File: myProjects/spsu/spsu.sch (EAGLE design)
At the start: 21 parts, among them IC1 MC34063A, J1 12V-in, J2 Hi-V, Q1 IRF840, X1 PJ-102A, X2 PJ-102A

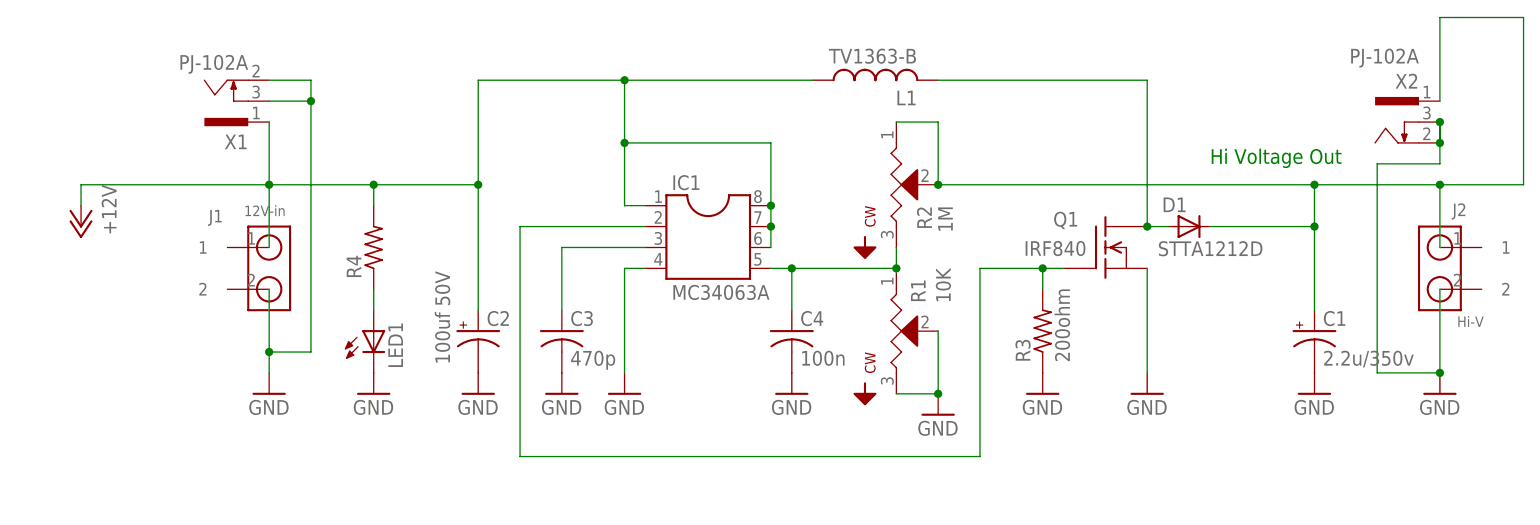
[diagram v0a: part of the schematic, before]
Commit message: removed power plugs and replaces with molex added Gerber files
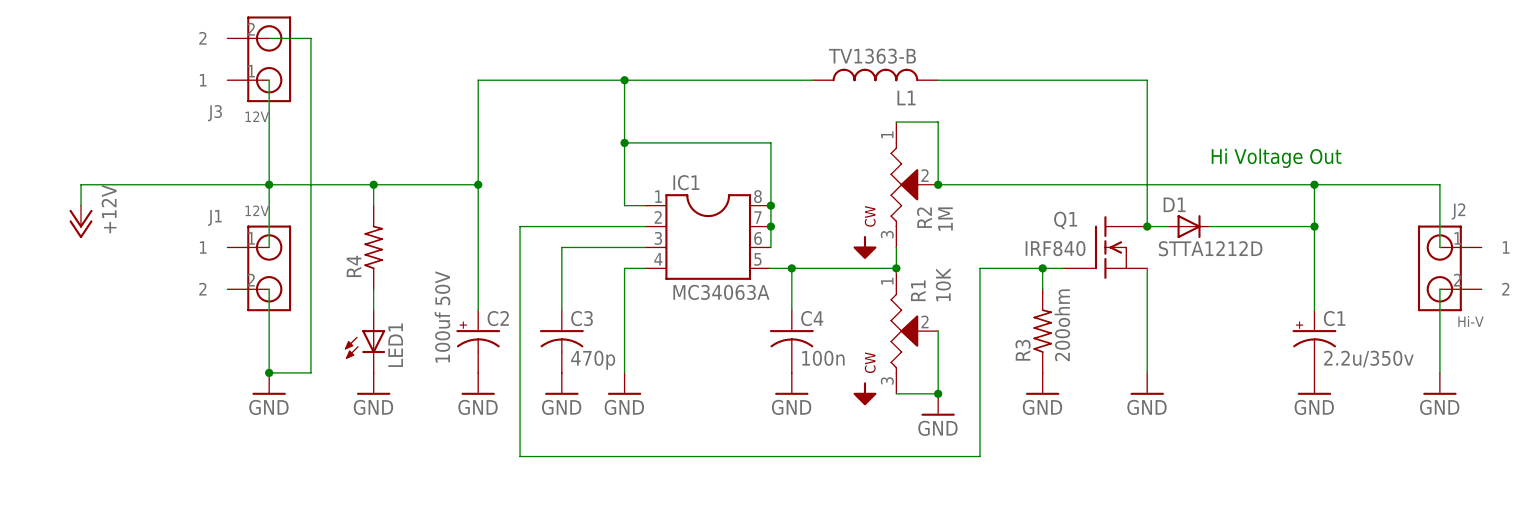
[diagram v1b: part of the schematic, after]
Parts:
- removed X1, X2: PJ-102A, kmarx1:PJ-102A
- added J3: 12V, kmarx1:MOLEX-2PIN-BASE
- J1: value 12V-in -> 12V
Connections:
- net +12V: now also J3.1; no longer X1.1
- net GND: now also J3.2; no longer X1.2, X1.3, X2.2, X2.3
- net HIVOLTAGEOUT: no longer X2.1
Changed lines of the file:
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@@
 <?xml version="1.0" encoding="utf-8"?>
 <!DOCTYPE eagle SYSTEM "eagle.dtd">
-<eagle version="6.0">
+<eagle version="6.1">
 <drawing>
 <settings>
@@
 <part name="R3" library="rcl" deviceset="R-US_" device="0204/5" value="200ohm"/>
 <part name="GND1" library="supply1" deviceset="GND" device=""/>
-<part name="J1" library="kmarx1" deviceset="MOLEX-2PIN-BASE" device="" value="12V-in"/>
+<part name="J1" library="kmarx1" deviceset="MOLEX-2PIN-BASE" device="" value="12V"/>
 <part name="J2" library="kmarx1" deviceset="MOLEX-2PIN-BASE" device="" value="Hi-V"/>
 <part name="GND2" library="supply1" deviceset="GND" device=""/>
@@
 <part name="H3" library="holes" deviceset="MOUNT-HOLE" device="3.0"/>
 <part name="H4" library="holes" deviceset="MOUNT-HOLE" device="3.0"/>
-<part name="X1" library="kmarx1" deviceset="PJ-102*" device="" technology="A"/>
-<part name="X2" library="kmarx1" deviceset="PJ-102*" device="" technology="A"/>
 <part name="LED1" library="led" deviceset="LED" device="3MM"/>
 <part name="GND11" library="supply1" deviceset="GND" device=""/>
 <part name="R4" library="rcl" deviceset="R-US_" device="0204/5"/>
+<part name="J3" library="kmarx1" deviceset="MOLEX-2PIN-BASE" device="" value="12V"/>
 </parts>
 <sheets>
@@
 <instance part="H3" gate="G$1" x="7.62" y="15.24"/>
 <instance part="H4" gate="G$1" x="7.62" y="7.62"/>
-<instance part="X1" gate="G$1" x="63.5" y="114.3" rot="R180"/>
-<instance part="X2" gate="G$1" x="205.74" y="111.76" smashed="yes" rot="MR0">
-<attribute name="NAME" x="208.28" y="115.824" size="1.778" layer="95" rot="MR0"/>
-<attribute name="VALUE" x="208.28" y="118.872" size="1.778" layer="96" rot="MR0"/>
-</instance>
 <instance part="LED1" gate="G$1" x="81.28" y="86.36"/>
 <instance part="GND11" gate="1" x="81.28" y="78.74"/>
 <instance part="R4" gate="G$1" x="81.28" y="96.52" rot="R90"/>
+<instance part="J3" gate="G$1" x="68.58" y="119.38" smashed="yes" rot="MR180">
+<attribute name="NAME" x="62.992" y="112.268" size="1.524" layer="95" font="vector" rot="MR0"/>
+<attribute name="VALUE" x="65.532" y="113.03" size="1.27" layer="95" font="vector" rot="MR180"/>
+</instance>
 </instances>
 <busses>
@@
 </segment>
 <segment>
-<wire x1="68.58" y1="116.84" x2="73.66" y2="116.84" width="0.1524" layer="91"/>
-<wire x1="73.66" y1="116.84" x2="73.66" y2="114.3" width="0.1524" layer="91"/>
-<wire x1="73.66" y1="114.3" x2="73.66" y2="83.82" width="0.1524" layer="91"/>
-<wire x1="68.58" y1="91.44" x2="68.58" y2="83.82" width="0.1524" layer="91"/>
-<wire x1="68.58" y1="83.82" x2="68.58" y2="81.28" width="0.1524" layer="91"/>
-<wire x1="73.66" y1="83.82" x2="68.58" y2="83.82" width="0.1524" layer="91"/>
-<wire x1="68.58" y1="114.3" x2="73.66" y2="114.3" width="0.1524" layer="91"/>
-<junction x="68.58" y="83.82"/>
-<junction x="73.66" y="114.3"/>
+<wire x1="68.58" y1="91.44" x2="68.58" y2="81.28" width="0.1524" layer="91"/>
 <pinref part="GND10" gate="1" pin="GND"/>
 <pinref part="J1" gate="G$1" pin="2"/>
-<pinref part="X1" gate="G$1" pin="2"/>
-<pinref part="X1" gate="G$1" pin="3"/>
-</segment>
-<segment>
-<wire x1="210.82" y1="111.76" x2="210.82" y2="109.22" width="0.1524" layer="91"/>
-<wire x1="210.82" y1="109.22" x2="210.82" y2="106.68" width="0.1524" layer="91"/>
-<wire x1="210.82" y1="106.68" x2="203.2" y2="106.68" width="0.1524" layer="91"/>
-<wire x1="203.2" y1="106.68" x2="203.2" y2="81.28" width="0.1524" layer="91"/>
+<pinref part="J3" gate="G$1" pin="2"/>
+<wire x1="68.58" y1="121.92" x2="73.66" y2="121.92" width="0.1524" layer="91"/>
+<wire x1="73.66" y1="121.92" x2="73.66" y2="81.28" width="0.1524" layer="91"/>
+<wire x1="73.66" y1="81.28" x2="68.58" y2="81.28" width="0.1524" layer="91"/>
+<junction x="68.58" y="81.28"/>
+</segment>
+<segment>
 <wire x1="210.82" y1="91.44" x2="210.82" y2="81.28" width="0.1524" layer="91"/>
-<wire x1="203.2" y1="81.28" x2="210.82" y2="81.28" width="0.1524" layer="91"/>
-<wire x1="210.82" y1="111.76" x2="210.82" y2="109.22" width="0.1524" layer="91"/>
-<junction x="210.82" y="81.28"/>
-<junction x="210.82" y="109.22"/>
-<junction x="210.82" y="111.76"/>
 <pinref part="GND1" gate="1" pin="GND"/>
 <pinref part="J2" gate="G$1" pin="2"/>
-<pinref part="X2" gate="G$1" pin="2"/>
-<pinref part="X2" gate="G$1" pin="3"/>
 </segment>
 <segment>
@@
 <segment>
 <wire x1="45.72" y1="101.6" x2="45.72" y2="104.14" width="0.1524" layer="91"/>
-<wire x1="68.58" y1="111.76" x2="68.58" y2="104.14" width="0.1524" layer="91"/>
 <wire x1="68.58" y1="104.14" x2="68.58" y2="96.52" width="0.1524" layer="91"/>
 <wire x1="45.72" y1="104.14" x2="68.58" y2="104.14" width="0.1524" layer="91"/>
@@
 <pinref part="C2" gate="G$1" pin="+"/>
 <pinref part="J1" gate="G$1" pin="1"/>
-<pinref part="X1" gate="G$1" pin="1"/>
 <pinref part="R4" gate="G$1" pin="2"/>
+<pinref part="J3" gate="G$1" pin="1"/>
+<wire x1="68.58" y1="116.84" x2="68.58" y2="104.14" width="0.1524" layer="91"/>
 </segment>
 </net>
 <net name="HIVOLTAGEOUT" class="0">
 <segment>
-<wire x1="210.82" y1="114.3" x2="210.82" y2="124.46" width="0.1524" layer="91"/>
-<wire x1="210.82" y1="124.46" x2="220.98" y2="124.46" width="0.1524" layer="91"/>
-<wire x1="220.98" y1="124.46" x2="220.98" y2="104.14" width="0.1524" layer="91"/>
 <wire x1="182.88" y1="99.06" x2="195.58" y2="99.06" width="0.1524" layer="91"/>
 <wire x1="195.58" y1="99.06" x2="195.58" y2="88.9" width="0.1524" layer="91"/>
@@
 <wire x1="144.78" y1="111.76" x2="149.86" y2="111.76" width="0.1524" layer="91"/>
 <wire x1="149.86" y1="111.76" x2="149.86" y2="104.14" width="0.1524" layer="91"/>
-<wire x1="220.98" y1="104.14" x2="210.82" y2="104.14" width="0.1524" layer="91"/>
 <junction x="195.58" y="99.06"/>
 <junction x="195.58" y="104.14"/>
 <junction x="149.86" y="104.14"/>
-<junction x="210.82" y="104.14"/>
 <pinref part="C1" gate="G$1" pin="+"/>
 <pinref part="D1" gate="G$1" pin="C"/>
@@
 <pinref part="R2" gate="G$1" pin="2"/>
 <pinref part="J2" gate="G$1" pin="1"/>
-<pinref part="X2" gate="G$1" pin="1"/>
 </segment>
 </net>
@@
 </sheet>
 </sheets>
+<errors>
+</errors>
 </schematic>
 </drawing>
